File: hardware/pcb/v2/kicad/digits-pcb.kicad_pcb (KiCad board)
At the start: 2 copper layers, 76.2 x 56.9 mm, 76 parts, among them J1 Conn_02x20_Odd_Even, J3 VIN_BARREL_PIGTAIL, J4 Conn_01x07, J6 Conn_01x02, J7 Screw_Terminal_01x02, J8 Conn_01x04, J9 Conn_01x03, SW1 SW_Push, U1 LM2596S-5, U2 DRV8871DDAR, U3 RP2040, U4 W25Q16JVSSIQ, U5 AMS1117-3.3, U6 TLV320AIC3104IRHBR, U7 XC6206P182MR, Y1 ABM8-272-T3

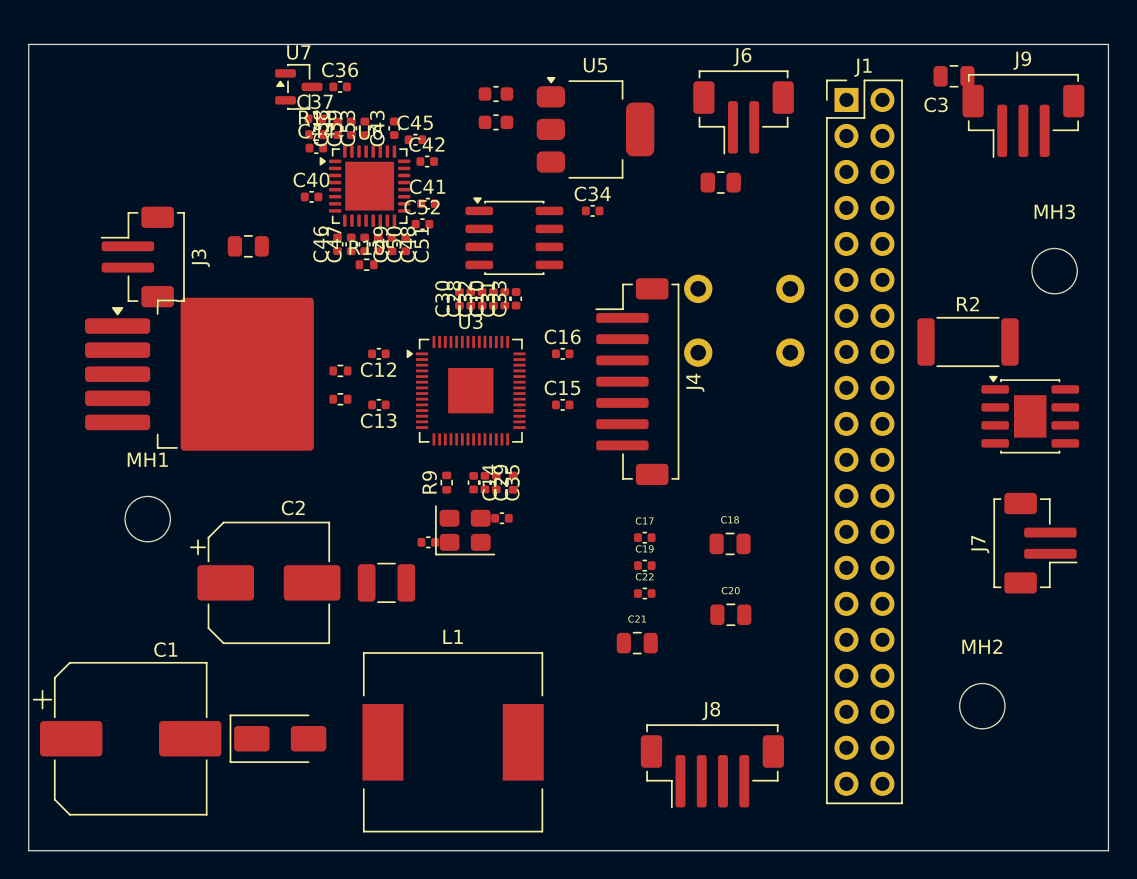
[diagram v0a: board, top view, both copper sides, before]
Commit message: feat(hardware): cluster placement validation, buck rework, schematic cleanup
Validation scripts and target files (Phase 5 prep):
- buck_targets.json + check_buck_placement.py (LM2596 switching loop)
- flash_targets.json + check_flash_placement.py (W25Q16 QSPI near RP2040)
- crystal_targets.json + check_crystal_placement.py (Y1 near RP2040 XIN)
- All targets calibrated against actual footprint geometry, not textbook ideals

Net classes:
- Power class: track 0.75mm, clearance 0.2mm, via 0.8/0.4mm
- Added +3V3, VIN_RAW, DVDD_1V1 to Power patterns

Schematic cleanup:
- Delete R3/R4: USB series resistors with floating pins (unused USB path;
  RP2040 reachable via UART_TX_PI/UART_RX_PI and SWD from the Pi)
- Delete C17-C22: orphan +3V3 bulk caps with no IC association, leftover
  from pre-codec-rebuild
- Add no_connect flags on U3.46 (USB_DM) and U3.47 (USB_DP)
- Remove dangling labels left by deleted components

PCB placement fixes:
- Buck cluster (U1/L1/D1/C1/C2/C4) relayed with correct pin orientation;
  U1 rot +90, L1 rot -90, C4 placed near U1.1
- Y1/C5/C6 crystal cluster shifted 1.5mm north toward U3 XIN
- 28 starter traces on F.Cu locked in place for RP2040 and codec
  close-in decoupling, with GND pours on F.Cu/B.Cu

Placement validation:
- Codec: 20/20 PASS
- RP2040: 16/16 PASS
- Buck: 5/5 PASS
- Flash: 2/2 PASS (C34 target relaxed 2.0 -> 3.5mm for SOIC-8 geometry)
- Crystal: 3/3 PASS

ERC: 0 errors, 71 warnings (all lib_symbol_mismatch / pre-existing).
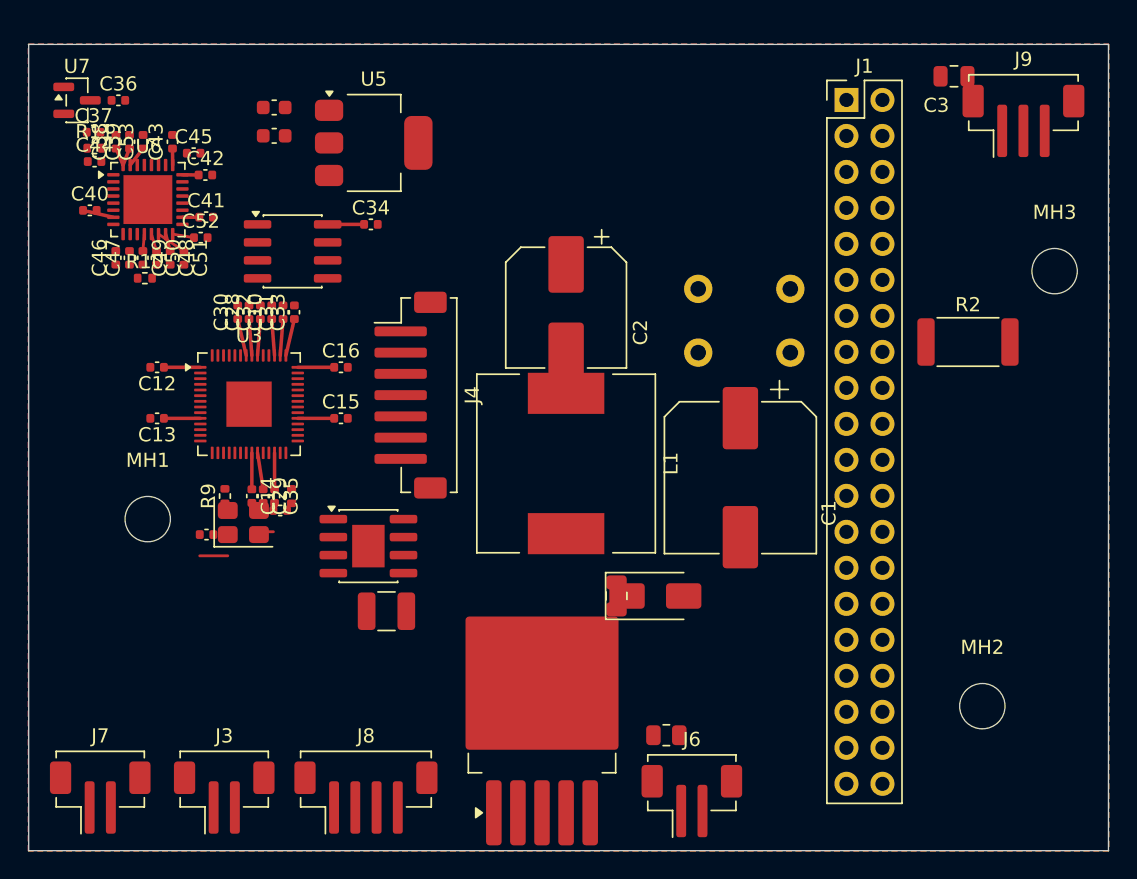
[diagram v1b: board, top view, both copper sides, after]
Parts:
- removed C17, C19, C22: 10uF, Capacitor_SMD:C_0402_1005Metric
- removed C18, C20, C21: 100nF, Capacitor_SMD:C_0805_2012Metric
- removed R3, R4: 27, Resistor_SMD:R_0402_1005Metric
- moved J7 68.7 mm to (20.1, 67.6), turned to 0 degrees
- moved J6 48.4 mm to (61.8, 67.9)
- moved U2 47.6 mm to (39.0, 49.9)
- moved C1 46.8 mm to (65.2, 45.0), turned to -90 degrees
- moved R1 39.2 mm to (60.0, 63.2)
- moved J3 38.6 mm to (28.8, 67.6), turned to 0 degrees
- moved C4 35.8 mm to (56.5, 53.4), turned to 90 degrees
- moved U1 32.3 mm to (51.2, 61.0), turned to 90 degrees
- moved C2 28.6 mm to (52.9, 33.0), turned to -90 degrees
- moved D1 28.3 mm to (59.2, 53.4)
- moved J8 24.5 mm to (38.8, 67.6)
- moved L1 21.2 mm to (52.9, 44.0), turned to -90 degrees
- moved C15 15.7 mm to (37.0, 40.8)
- moved C16 15.7 mm to (37.0, 37.2)
- moved R5 15.7 mm to (33.5, 46.3)
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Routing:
- net +3V3: track 0.00 -> 31.5 mm
- net DVDD_1V1: track 0.00 -> 7.82 mm
- net RUN: track 0.00 -> 2.57 mm
- net /codec/+1V8: track 0.00 -> 2.52 mm
- net /codec/MIC2L_INT: track 0.00 -> 2.15 mm
- net XIN: track 0.00 -> 1.98 mm
- net /codec/MIC2R_INT: track 0.00 -> 1.52 mm
- net CODEC_RESET: track 0.00 -> 1.48 mm
- net /codec/MIC1RM_INT: track 0.00 -> 1.25 mm
- net /codec/MICBIAS: track 0.00 -> 1.24 mm
- net /codec/MIC1RP_INT: track 0.00 -> 1.19 mm
- net GND: track 0.00 -> 1.02 mm
- added copper zone on B.Cu, net GND
- added copper zone on F.Cu, net GND

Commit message: feat(hardware): place ringer cluster + C56 (Phase 4)
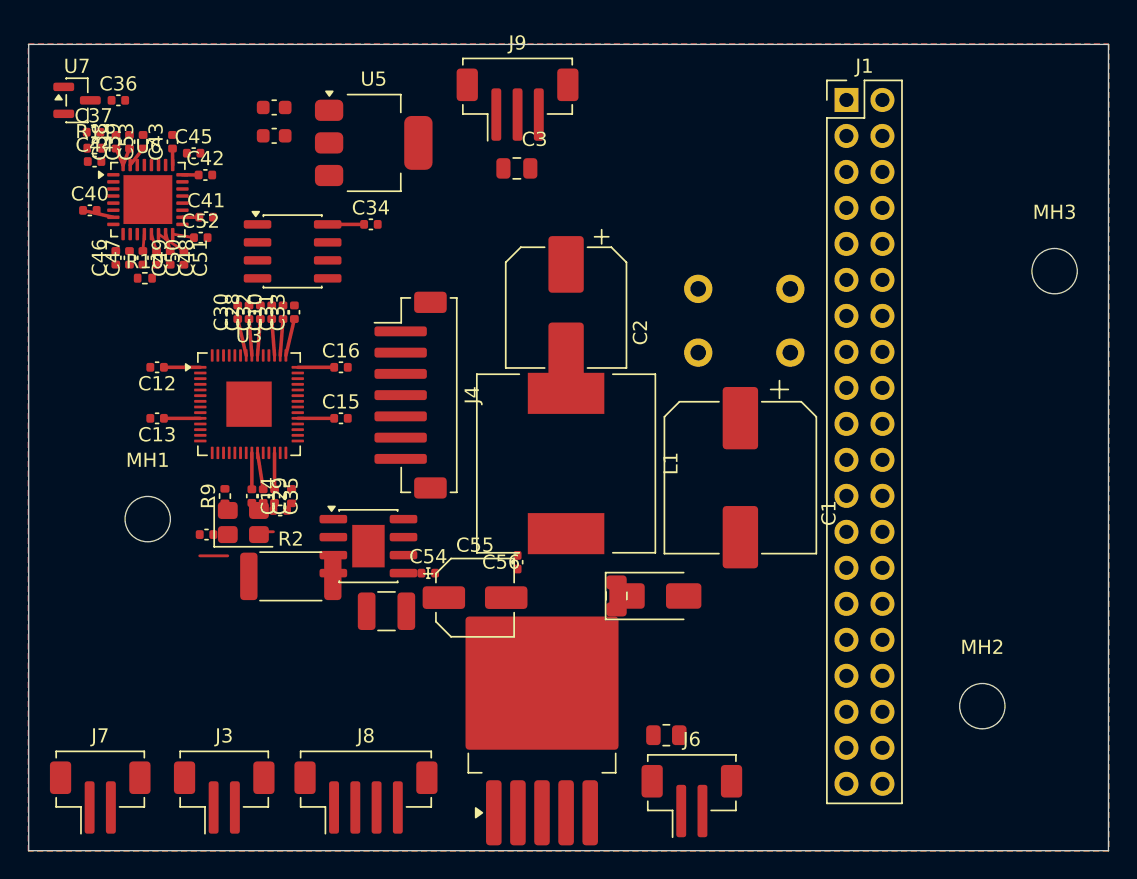
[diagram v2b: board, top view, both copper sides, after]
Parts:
- added C54: 100nF, Capacitor_SMD:C_0402_1005Metric, F.Cu at (43.2, 51.8)
- added C55: 47uF, Capacitor_SMD:CP_Elec_5x5.3, F.Cu at (46.5, 53.5)
- added C56: 100nF, Capacitor_SMD:C_0402_1005Metric, F.Cu at (49.5, 51.0)
- moved R2 50.6 mm to (33.5, 52.0)
- moved J9 35.7 mm to (49.5, 18.7)
- moved C3 31.5 mm to (49.5, 23.2), turned to 0 degrees

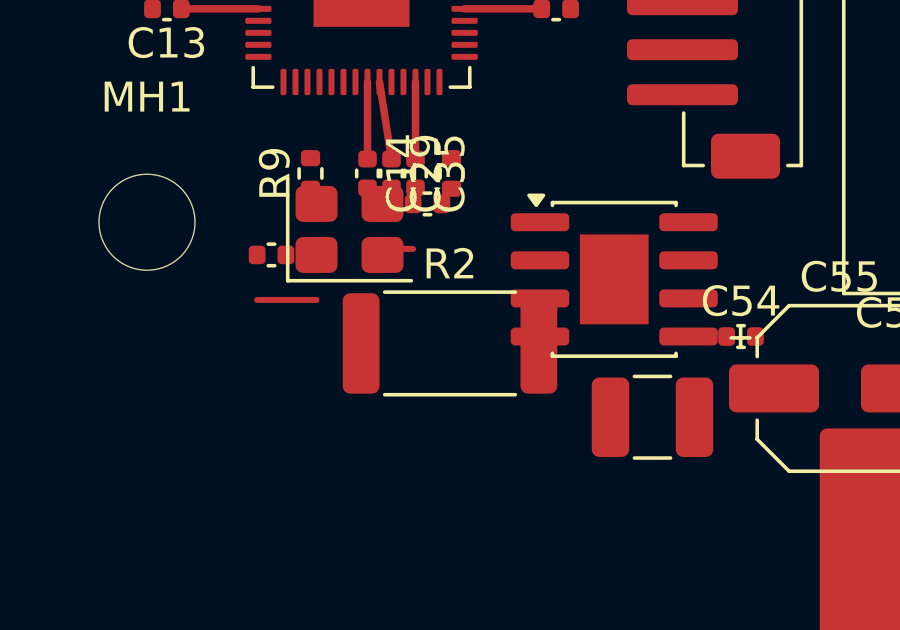
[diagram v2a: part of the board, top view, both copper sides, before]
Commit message: fix(hardware): R2 ILIM footprint 2512 -> 0402 to match ringer sheet spec
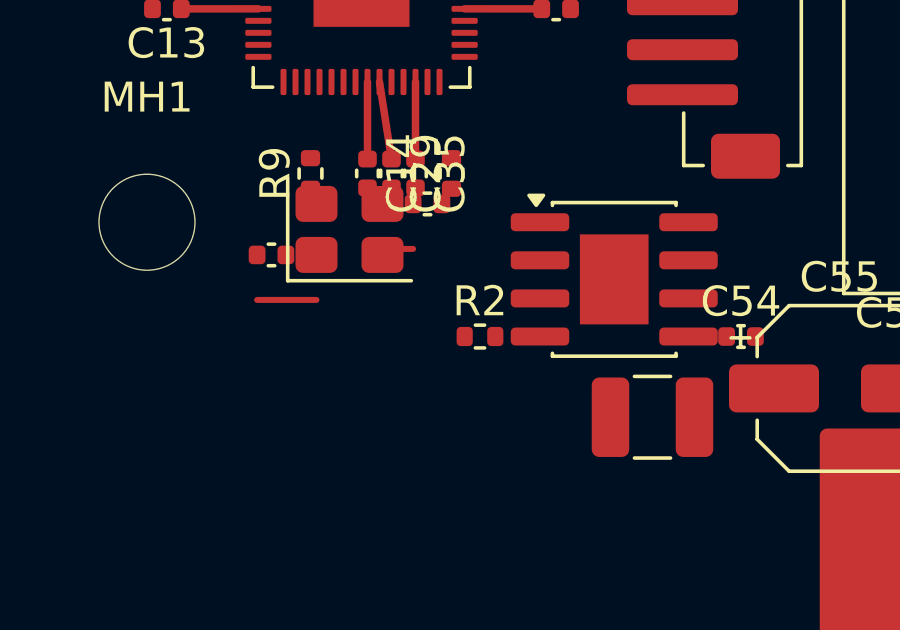
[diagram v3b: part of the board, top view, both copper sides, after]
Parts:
- R2: footprint Resistor_SMD:R_2512_6332Metric -> Resistor_SMD:R_0402_1005Metric
- moved R2 1.03 mm to (34.5, 51.8)

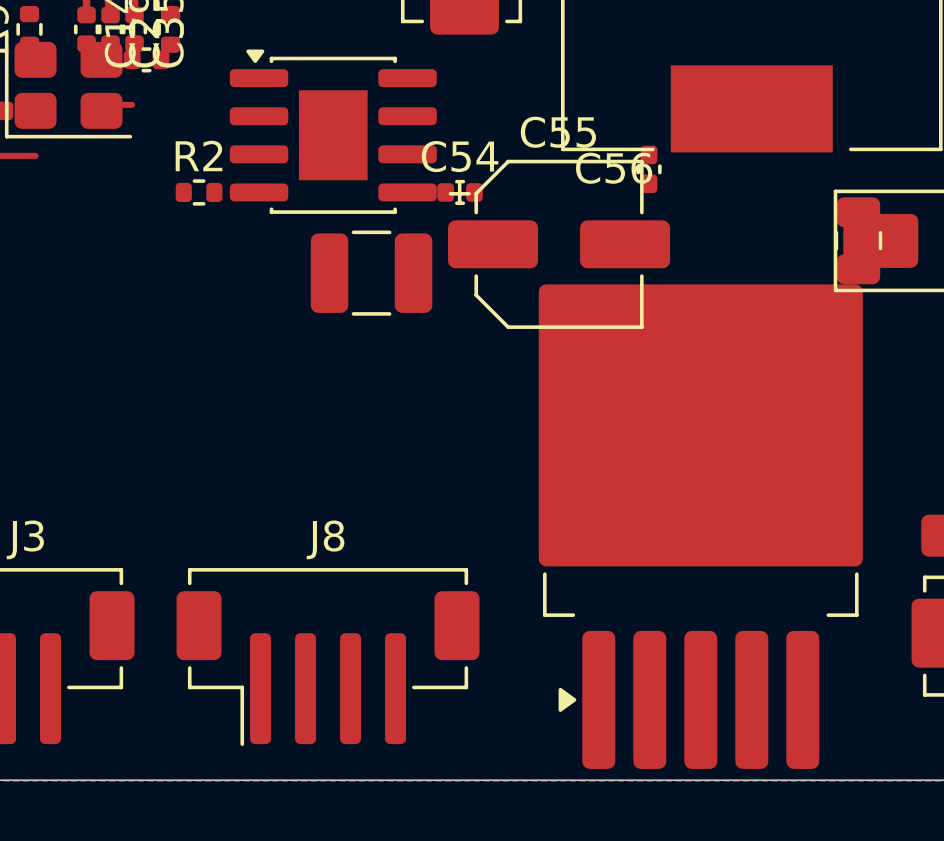
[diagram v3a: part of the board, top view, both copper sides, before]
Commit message: feat(hardware): route ringer cluster + C56 close-in decoupling (Phase 5)
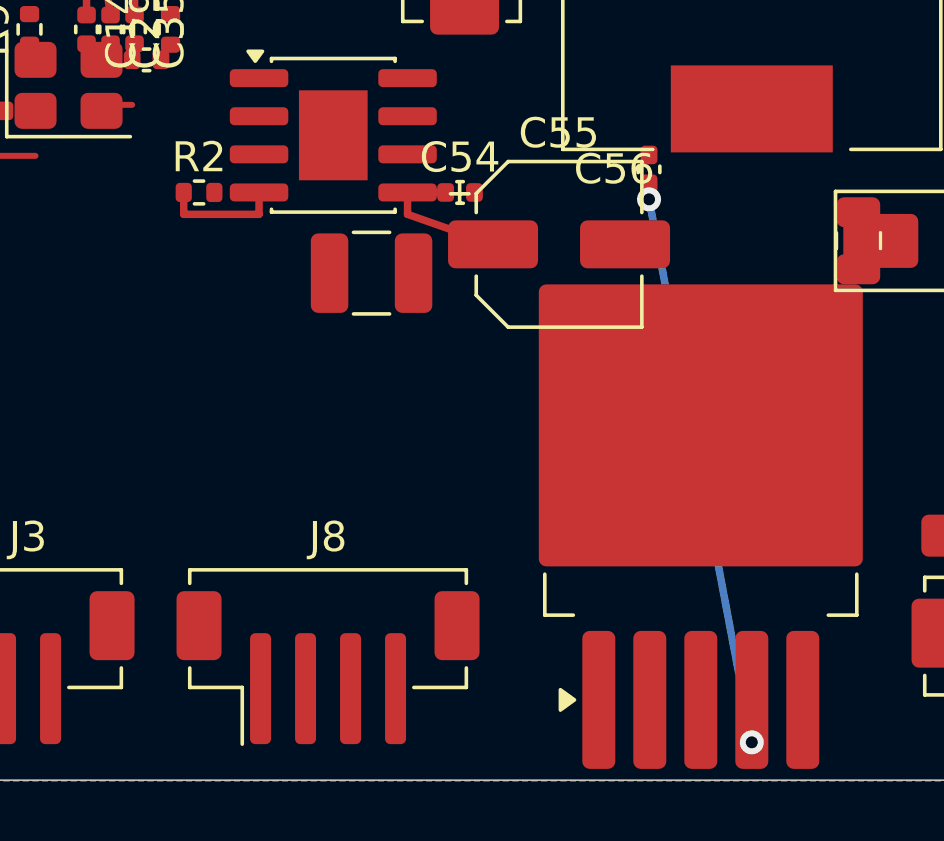
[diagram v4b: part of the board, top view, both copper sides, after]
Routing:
- net +5V: track 0.00 -> 20.4 mm, vias 0 -> 2
- net +12V: track 0.00 -> 5.02 mm
- net ILIM: track 0.00 -> 3.97 mm
